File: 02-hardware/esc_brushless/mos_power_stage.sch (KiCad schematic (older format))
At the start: 18 parts

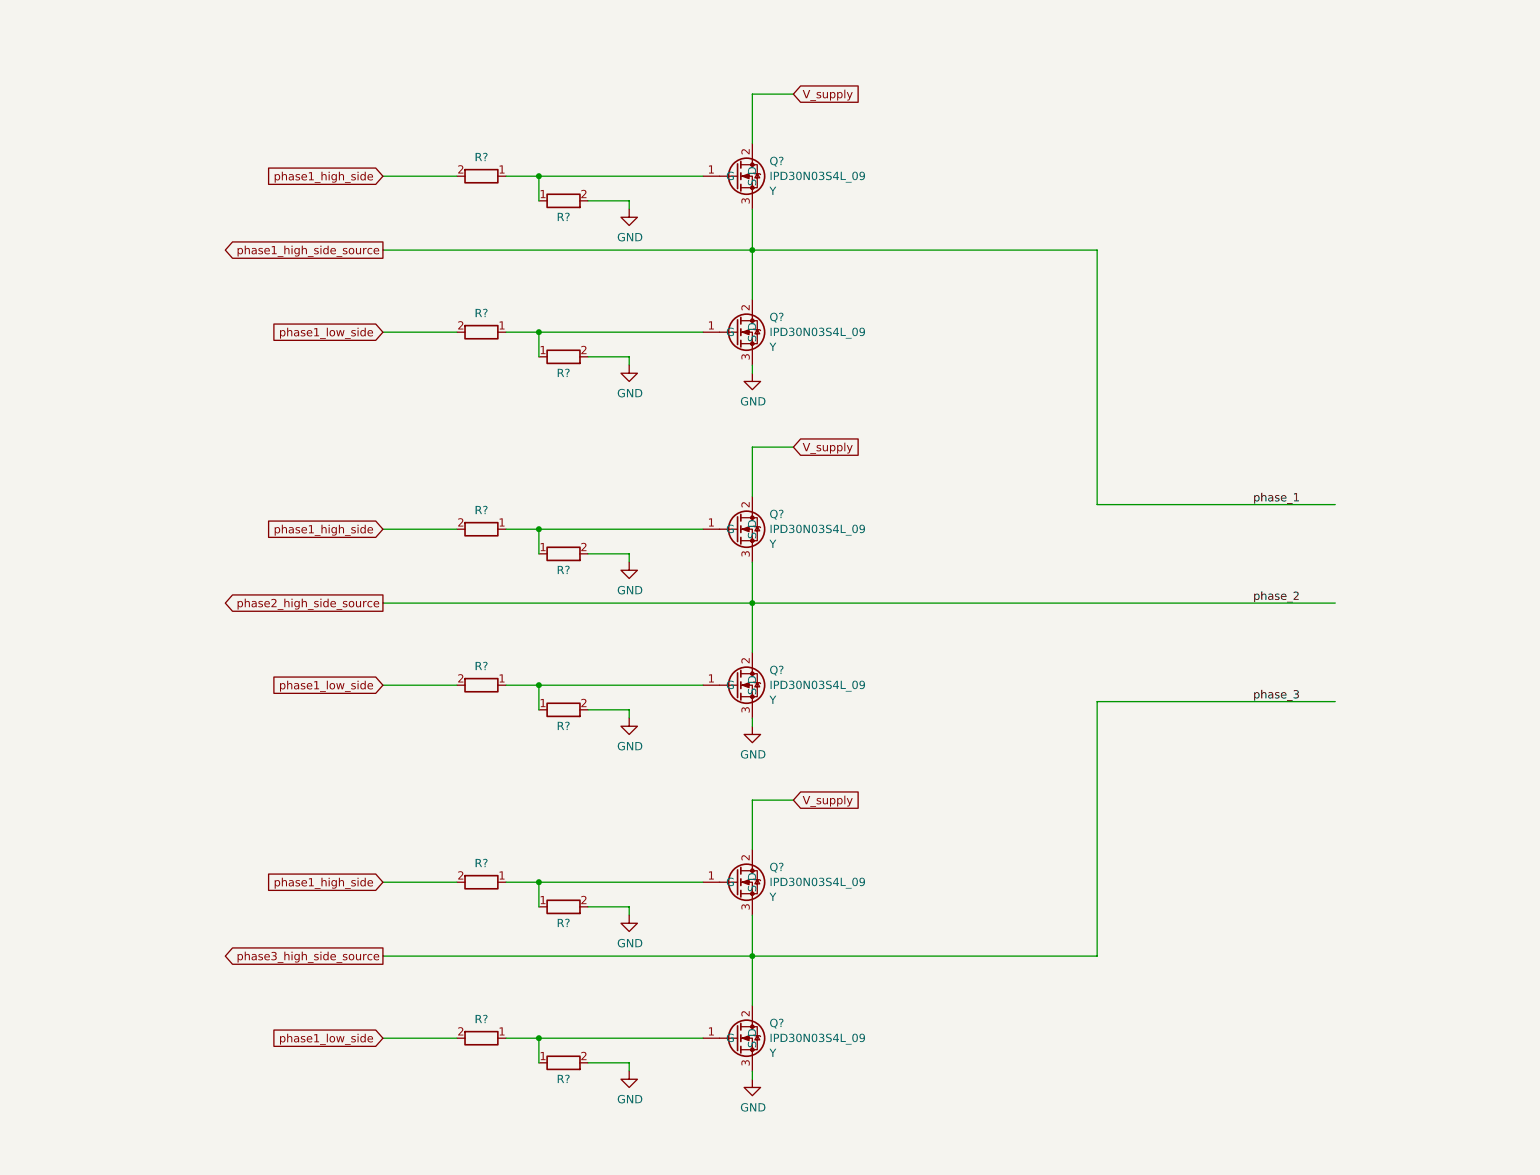
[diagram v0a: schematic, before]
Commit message: Schematics v1.0 - Architecture, MOS power stage, mos driver stage and RS485 interface
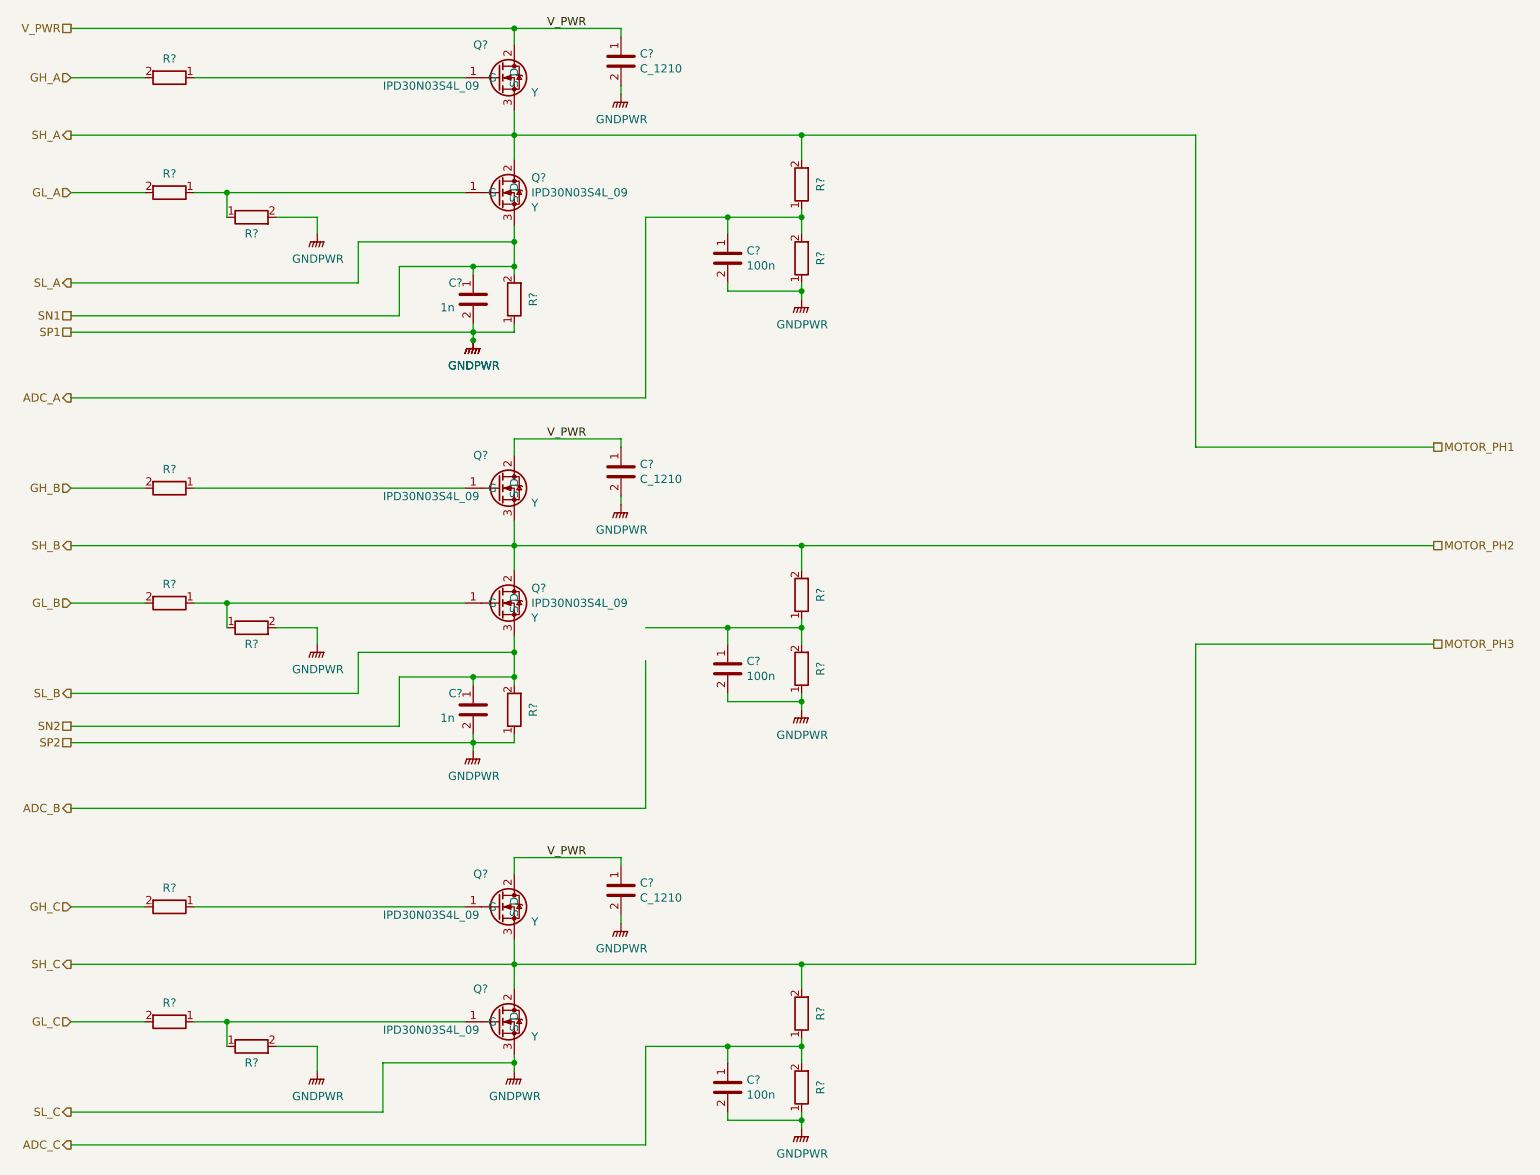
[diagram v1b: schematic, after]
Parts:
- removed Q? (x2): IPD30N03S4L_09, p_Package_TO_SMD:TO-252-pin_1_3_TabPin2, symbol p_Transistor_FET:IPD30N03S4L_09
- removed R? (x3): R_0603, p_Package_Resistor_SMD:R_0603_1608Metric_Pad0.98x0.95mm_HandSolder, symbol p_Passive:R_0603
- added C? (x3): C_1210, p_Package_Capacitor_SMD:C_1210_3225Metric_Pad1.33x2.70mm_HandSolder, symbol p_Passive:C_1210
- added C? (x3): 100n, p_Package_Capacitor_SMD:C_0805_2012Metric_Pad1.18x1.45mm_HandSolder, symbol p_Passive:C_0805
- added C? (x2): 1n, p_Package_Capacitor_SMD:C_0603_1608Metric_Pad1.08x0.95mm_HandSolder, symbol p_Passive:C_0603
- added Q? (x2): IPD30N03S4L_09, p_Package_TO_SMD:TO-252-pin_1_3_TabPin2, symbol p_Transistor_FET:IPD30N03S4L_09
- added R? (x8): R_0603, p_Package_Resistor_SMD:R_0603_1608Metric_Pad0.98x0.95mm_HandSolder, symbol p_Passive:R_0603
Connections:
- net labels added: ADC_A, ADC_B, ADC_C, GH_A, GH_B, GH_C, GL_A, GL_B, GL_C, GNDPWR, MOTOR_PH1, MOTOR_PH2, MOTOR_PH3, SH_A, SH_B, SH_C, SL_A, SL_B, SL_C, SN1, SN2, SP1, SP2, V_PWR
- net labels removed: GND, V_supply, phase1_high_side, phase1_high_side_source, phase1_low_side, phase2_high_side_source, phase3_high_side_source, phase_1, phase_2, phase_3
- wire segments 61 -> 129
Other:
- moved on the sheet: Q?, R?

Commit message: Schematics v1.0 - Architecture, microcontroler, global interconnections and IO
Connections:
- net ADC_B: now also C?.1, R?.1, R?.2
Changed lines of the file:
@@
 	1700 5400 5200 5400
-Wire Wire Line
-	5200 4500 5200 5400
 Wire Wire Line
 	4400 1300 6150 1300
@@
 Wire Wire Line
 	8550 4400 8550 6350
+Wire Wire Line
+	5200 4300 5200 5400
+Text HLabel 10000 5550 2    50   UnSpc ~ 0
+GND_PWR
+$Comp
+L power:GNDPWR #PWR?
+U 1 1 60A0362A
+P 9900 5650
+AR Path="/603415C7/60A0362A" Ref="#PWR?"  Part="1"
+AR Path="/602453F4/60A0362A" Ref="#PWR?"  Part="1"
+F 0 "#PWR?" H 9900 5450 50  0001 C CNN
+F 1 "GNDPWR" H 9904 5496 50  0000 C CNN
+F 2 "" H 9900 5600 50  0001 C CNN
+F 3 "" H 9900 5600 50  0001 C CNN
+	1    9900 5650
+	1    0    0    -1
+$EndComp
+Wire Wire Line
+	10000 5550 9900 5550
+Wire Wire Line
+	9900 5550 9900 5650
 $EndSCHEMATC

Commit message: Schematics v1.0 - Fix DRC issues
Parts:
- gave numbers to parts that had none: 31

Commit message: Schematics v1.0 - PCB layout v1.0
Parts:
- removed R18, R19: R_0603, p_Package_Resistor_SMD:R_0603_1608Metric_Pad0.98x0.95mm_HandSolder, symbol p_Passive:R_0603
- added R18, R19: R_shunt_2512, p_Package_Resistor_SMD:R_2512_6332Metric_shunt, symbol p_Passive:R_shunt_2512
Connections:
- net GNDPWR: now also R18.2, R19.2; no longer C1.2, C2.2
- net SL_A: now also R18.1; no longer C1.1
- net SL_B: now also R19.1; no longer C2.1
- new net SN1: C1.1, R18.3
- new net SN2: C2.1, R19.3
- new net SP1: C1.2, R18.4
- new net SP2: C2.2, R19.4
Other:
- moved on the sheet: C2
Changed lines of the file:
@@
 Wire Wire Line
 	1700 6350 4400 6350
-$Comp
-L power:GNDPWR #PWR?
-U 1 1 6057A563
-P 4150 2550
-AR Path="/603415C7/6057A563" Ref="#PWR?"  Part="1"
-AR Path="/602453F4/6057A563" Ref="#PWR018"  Part="1"
-F 0 "#PWR018" H 4150 2350 50  0001 C CNN
-F 1 "GNDPWR" H 4154 2396 50  0000 C CNN
-F 2 "" H 4150 2500 50  0001 C CNN
-F 3 "" H 4150 2500 50  0001 C CNN
-	1    4150 2550
-	1    0    0    -1
-$EndComp
 Text HLabel 1700 2400 0    50   UnSpc ~ 0
 SN1
@@
 Wire Wire Line
 	8550 1300 8550 3200
-$Comp
-L p_Passive:R_0603 R18
-U 1 1 60620400
-P 4400 2300
-F 0 "R18" V 4285 2300 50  0000 C CNN
-F 1 "R_0603" V 4284 2300 50  0001 C CNN
-F 2 "p_Package_Resistor_SMD:R_0603_1608Metric_Pad0.98x0.95mm_HandSolder" H 4400 2300 50  0001 C CNN
-F 3 "" H 4400 2300 50  0001 C CNN
-	1    4400 2300
-	-1   0    0    1
-$EndComp
-$Comp
-L p_Passive:C_0603 C1
-U 1 1 60622C1C
-P 4150 2300
-F 0 "C1" H 4000 2400 50  0000 L CNN
-F 1 "1n" H 3950 2250 50  0000 L CNN
-F 2 "p_Package_Capacitor_SMD:C_0603_1608Metric_Pad1.08x0.95mm_HandSolder" H 4150 2300 50  0001 C CNN
-F 3 "" H 4150 2300 50  0001 C CNN
-	1    4150 2300
-	1    0    0    -1
-$EndComp
-Wire Wire Line
-	4150 2450 4150 2500
-Wire Wire Line
-	4400 2500 4400 2450
-Wire Wire Line
-	1700 2500 4150 2500
-Connection ~ 4150 2500
+Wire Wire Line
+	1700 2500 3850 2500
 Wire Wire Line
 	1700 2400 3700 2400
@@
 L power:GNDPWR #PWR?
 U 1 1 6066931F
-P 4150 5050
+P 4400 5050
 AR Path="/603415C7/6066931F" Ref="#PWR?"  Part="1"
 AR Path="/602453F4/6066931F" Ref="#PWR020"  Part="1"
-F 0 "#PWR020" H 4150 4850 50  0001 C CNN
-F 1 "GNDPWR" H 4154 4896 50  0000 C CNN
-F 2 "" H 4150 5000 50  0001 C CNN
-F 3 "" H 4150 5000 50  0001 C CNN
-	1    4150 5050
-	1    0    0    -1
-$EndComp
-$Comp
-L p_Passive:R_0603 R19
-U 1 1 60669326
-P 4400 4800
-F 0 "R19" V 4285 4800 50  0000 C CNN
-F 1 "R_0603" V 4284 4800 50  0001 C CNN
-F 2 "p_Package_Resistor_SMD:R_0603_1608Metric_Pad0.98x0.95mm_HandSolder" H 4400 4800 50  0001 C CNN
-F 3 "" H 4400 4800 50  0001 C CNN
-	1    4400 4800
-	-1   0    0    1
+F 0 "#PWR020" H 4400 4850 50  0001 C CNN
+F 1 "GNDPWR" H 4404 4896 50  0000 C CNN
+F 2 "" H 4400 5000 50  0001 C CNN
+F 3 "" H 4400 5000 50  0001 C CNN
+	1    4400 5050
+	1    0    0    -1
 $EndComp
 $Comp
 L p_Passive:C_0603 C2
 U 1 1 6066932C
-P 4150 4800
-F 0 "C2" H 4000 4900 50  0000 L CNN
-F 1 "1n" H 3950 4750 50  0000 L CNN
-F 2 "p_Package_Capacitor_SMD:C_0603_1608Metric_Pad1.08x0.95mm_HandSolder" H 4150 4800 50  0001 C CNN
-F 3 "" H 4150 4800 50  0001 C CNN
-	1    4150 4800
-	1    0    0    -1
-$EndComp
-Wire Wire Line
-	4150 4950 4150 5000
-Wire Wire Line
-	4400 5000 4400 4950
-Wire Wire Line
-	1700 5000 4150 5000
-Connection ~ 4150 5000
+P 4100 4750
+F 0 "C2" H 3950 4850 50  0000 L CNN
+F 1 "1n" H 3900 4700 50  0000 L CNN
+F 2 "p_Package_Capacitor_SMD:C_0603_1608Metric_Pad1.08x0.95mm_HandSolder" H 4100 4750 50  0001 C CNN
+F 3 "" H 4100 4750 50  0001 C CNN
+	1    4100 4750
+	1    0    0    -1
+$EndComp
 Wire Wire Line
 	3700 4900 3700 4600
-Wire Wire Line
-	1700 4900 3700 4900
 Wire Wire Line
 	2450 3450 4100 3450
@@
 Wire Wire Line
 	3200 4300 3200 4400
-Wire Wire Line
-	4150 5000 4400 5000
-Wire Wire Line
-	4150 5000 4150 5050
-Wire Wire Line
-	4150 2500 4400 2500
-Wire Wire Line
-	4150 2500 4150 2550
 Text HLabel 1700 4900 0    50   UnSpc ~ 0
 SN2
@@
 Wire Wire Line
 	6150 1300 8550 1300
-$Comp
-L power:GNDPWR #PWR?
-U 1 1 607193DC
-P 4150 2550
-AR Path="/603415C7/607193DC" Ref="#PWR?"  Part="1"
-AR Path="/602453F4/607193DC" Ref="#PWR019"  Part="1"
-F 0 "#PWR019" H 4150 2350 50  0001 C CNN
-F 1 "GNDPWR" H 4154 2396 50  0000 C CNN
-F 2 "" H 4150 2500 50  0001 C CNN
-F 3 "" H 4150 2500 50  0001 C CNN
-	1    4150 2550
-	1    0    0    -1
-$EndComp
 Text HLabel 1700 2900 0    50   Output ~ 0
 ADC_A
@@
 	4400 650  1700 650
 Connection ~ 4400 650
-Connection ~ 4150 2550
 Text HLabel 10000 3200 2    50   UnSpc ~ 0
 MOTOR_PH1
@@
 	3700 2100 3700 2400
 Wire Wire Line
-	3700 2100 4150 2100
-Wire Wire Line
-	4150 2100 4150 2150
-Wire Wire Line
-	4150 2100 4400 2100
-Wire Wire Line
-	4400 2100 4400 2150
-Connection ~ 4150 2100
-Wire Wire Line
-	4400 2100 4400 1950
-Connection ~ 4400 2100
-Connection ~ 4400 1950
-Wire Wire Line
-	4400 4650 4400 4600
-Wire Wire Line
-	4400 4600 4150 4600
-Wire Wire Line
-	4150 4600 4150 4650
-Wire Wire Line
-	3700 4600 4150 4600
-Connection ~ 4150 4600
-Wire Wire Line
 	4400 4350 4400 4450
-Connection ~ 4400 4600
 Wire Wire Line
 	4400 4450 3450 4450
@@
 Wire Wire Line
 	3450 4700 1700 4700
-Connection ~ 4400 4450
-Wire Wire Line
-	4400 4450 4400 4600
 Text HLabel 1700 2200 0    50   Output ~ 0
 SL_A
@@
 Wire Wire Line
 	9900 5550 9900 5650
+$Comp
+L p_Passive:R_shunt_2512 R19
+U 1 1 60B32745
+P 4400 4750
+F 0 "R19" H 4470 4750 50  0000 L CNN
+F 1 "R_shunt_2512" H 4470 4705 50  0001 L CNN
+F 2 "p_Package_Resistor_SMD:R_2512_6332Metric_shunt" H 4400 4750 50  0001 C CNN
+F 3 "" H 4400 4750 50  0001 C CNN
+	1    4400 4750
+	1    0    0    -1
+$EndComp
+Wire Wire Line
+	3700 4600 4100 4600
+Connection ~ 4100 4600
+Wire Wire Line
+	4100 4600 4250 4600
+Wire Wire Line
+	4250 4900 4100 4900
+Wire Wire Line
+	1700 4900 3700 4900
+Connection ~ 4100 4900
+Wire Wire Line
+	1700 5000 3850 5000
+Wire Wire Line
+	3850 5000 3850 4900
+Wire Wire Line
+	3850 4900 4100 4900
+Wire Wire Line
+	4400 5000 4400 5050
+Wire Wire Line
+	4400 4500 4400 4450
+Connection ~ 4400 4450
+$Comp
+L power:GNDPWR #PWR?
+U 1 1 60B6AA37
+P 4400 2550
+AR Path="/603415C7/60B6AA37" Ref="#PWR?"  Part="1"
+AR Path="/602453F4/60B6AA37" Ref="#PWR0110"  Part="1"
+F 0 "#PWR0110" H 4400 2350 50  0001 C CNN
+F 1 "GNDPWR" H 4404 2396 50  0000 C CNN
+F 2 "" H 4400 2500 50  0001 C CNN
+F 3 "" H 4400 2500 50  0001 C CNN
+	1    4400 2550
+	1    0    0    -1
+$EndComp
+Wire Wire Line
+	4400 2500 4400 2550
+Wire Wire Line
+	4400 2000 4400 1950
+Connection ~ 4400 1950
+Wire Wire Line
+	3850 2400 3850 2500
+Wire Wire Line
+	3700 2100 4100 2100
+Wire Wire Line
+	3850 2400 4100 2400
+$Comp
+L p_Passive:R_shunt_2512 R18
+U 1 1 60B9FD3E
+P 4400 2250
+F 0 "R18" H 4470 2250 50  0000 L CNN
+F 1 "R_shunt_2512" H 4470 2205 50  0001 L CNN
+F 2 "p_Package_Resistor_SMD:R_2512_6332Metric_shunt" H 4400 2250 50  0001 C CNN
+F 3 "" H 4400 2250 50  0001 C CNN
+	1    4400 2250
+	1    0    0    -1
+$EndComp
+$Comp
+L p_Passive:C_0603 C1
+U 1 1 60BA1C5D
+P 4100 2250
+F 0 "C1" H 3950 2350 50  0000 L CNN
+F 1 "1n" H 3900 2200 50  0000 L CNN
+F 2 "p_Package_Capacitor_SMD:C_0603_1608Metric_Pad1.08x0.95mm_HandSolder" H 4100 2250 50  0001 C CNN
+F 3 "" H 4100 2250 50  0001 C CNN
+	1    4100 2250
+	1    0    0    -1
+$EndComp
+Connection ~ 4100 2100
+Wire Wire Line
+	4100 2100 4250 2100
+Connection ~ 4100 2400
+Wire Wire Line
+	4100 2400 4250 2400
 $EndSCHEMATC
